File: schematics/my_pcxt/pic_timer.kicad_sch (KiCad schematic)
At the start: 4 parts, among them J3 Conn_02x40_Top_Bottom, P3 Conn_01x10, U15 8253, U7 8259A

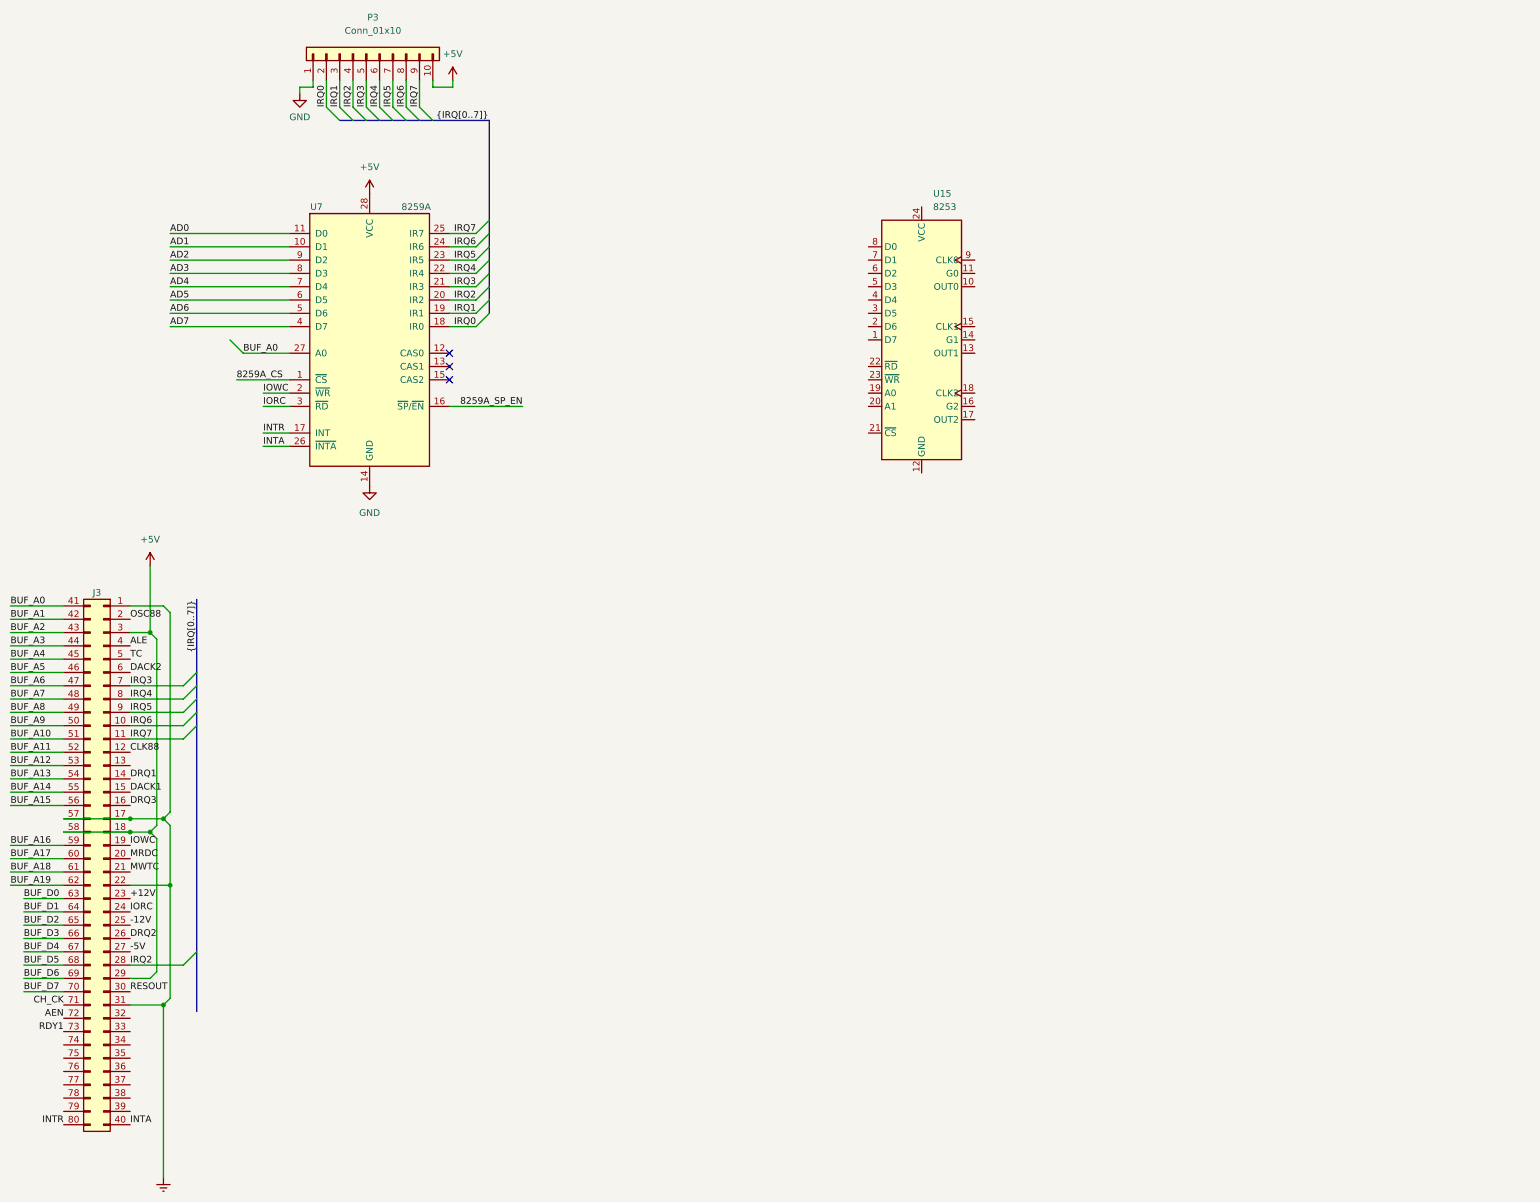
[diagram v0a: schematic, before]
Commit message: Implemented 8259 e 8253
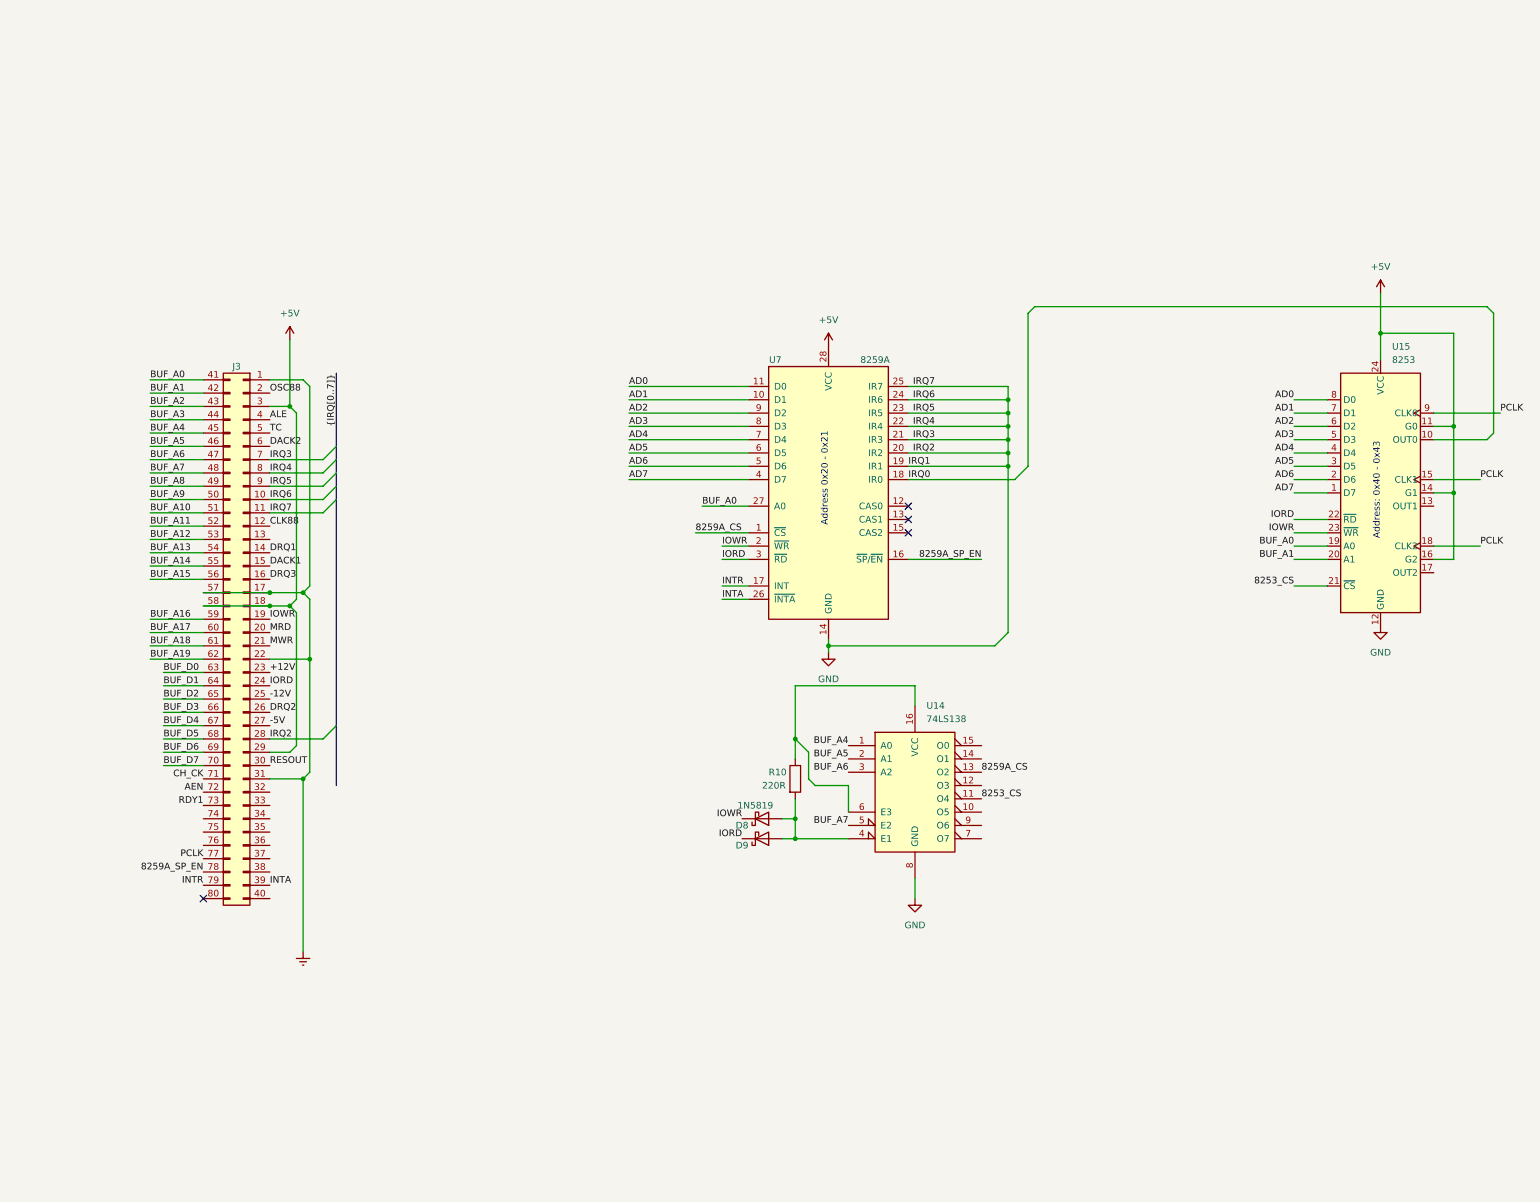
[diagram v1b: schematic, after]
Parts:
- removed P3: Conn_01x10, Connector_PinSocket_2.54mm:PinSocket_1x10_P2.54mm_Vertical, symbol Connector_Generic:Conn_01x10
- added D8, D9: 1N5819, Diode_THT:D_DO-41_SOD81_P10.16mm_Horizontal, symbol Diode:1N5819
- added R10: 220R, symbol Device:R
- added U14: 74LS138, symbol 74xx:74LS138
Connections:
- net IORC is gone; now on net IORD: J3.24 (Pin_24), U7.3 (~{RD})
- net IOWC is gone; now on net IOWR: J3.19 (Pin_19), U7.2 (~{WR})
- net IRQ1 is gone; now on net GND: U7.19 (IR1)
- net IRQ2 is gone; now on net GND: J3.28 (Pin_28), U7.20 (IR2)
- net IRQ3 is gone; now on net GND: J3.7 (Pin_7), U7.21 (IR3)
- net IRQ4 is gone; now on net GND: J3.8 (Pin_8), U7.22 (IR4)
- net IRQ5 is gone; now on net GND: J3.9 (Pin_9), U7.23 (IR5)
- net IRQ6 is gone; now on net GND: J3.10 (Pin_10), U7.24 (IR6)
- net IRQ7 is gone; now on net GND: J3.11 (Pin_11), U7.25 (IR7)
- net +5V: now also U15.11 (G0), U15.14 (G1), U15.16 (G2), U15.24 (VCC)
- net 8259A_CS: now also U14.13 (O2)
- net 8259A_SP_EN: now also J3.78 (Pin_78)
- net AD0: now also U15.8 (D0)
- net AD1: now also U15.7 (D1)
- net AD2: now also U15.6 (D2)
- net AD3: now also U15.5 (D3)
- net AD4: now also U15.4 (D4)
- net AD5: now also U15.3 (D5)
- net AD6: now also U15.2 (D6)
- net AD7: now also U15.1 (D7)
- net BUF_A0: now also U15.19 (A0)
- net BUF_A1: now also U15.20 (A1)
- net BUF_A4: now also U14.1 (A0)
- net BUF_A5: now also U14.2 (A1)
- net BUF_A6: now also U14.3 (A2)
- net BUF_A7: now also U14.5 (E2)
- net GND: now also U15.12 (GND), U14.8 (GND)
- net INTA: now also J3.39 (Pin_39); no longer J3.40 (Pin_40)
- net INTR: now also J3.79 (Pin_79); no longer J3.80 (Pin_80)
- net IRQ0: now also U15.10 (OUT0)
- net PCLK: now reaches U15.15 (CLK1)
- net PCLK: now also J3.77 (Pin_77), U15.18 (CLK2), U15.9 (CLK0)
- net 8253_CS: now reaches U15.21 (~{CS})
- net 8253_CS: now also U14.11 (O4)
- net IORD: now reaches U15.22 (~{RD})
- net IORD: now also D9.1 (K)
- net IOWR: now reaches U15.23 (~{WR})
- net IOWR: now also D8.1 (K)
- net MRDC renamed MRD
- net MWTC renamed MWR
- new net: R10.1, U14.16 (VCC), U14.6 (E3)
- new net: D8.2 (A), D9.2 (A), R10.2, U14.4 (E1)
- no-connect marks 3 -> 4
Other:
- note added: "Address 0x20 - 0x21"
- note added: "Address: 0x40 - 0x43"
- moved on the sheet: J3, U15, U7

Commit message: Updating schematics
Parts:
- removed D8, D9: 1N5819, Diode_THT:D_DO-41_SOD81_P10.16mm_Horizontal, symbol Diode:1N5819
- removed R10: 220R, symbol Device:R
- removed U14: 74LS138, symbol 74xx:74LS138
- added C12: 100nF, symbol Device:C
- added C19, C20, C21, C2VS+1, C2VS-1: 1uF, symbol Device:C_Polarized
- added D10, D5: 1N5819, Diode_THT:D_DO-41_SOD81_P10.16mm_Horizontal, symbol Diode:1N5819
- added J5: DE9_Plug, symbol Connector:DE9_Plug
- added R2: 270R, symbol Device:R
- added U14: 16550, Package_DIP:DIP-40_W15.24mm, symbol Interface_UART:16550
- added U23: DTE, symbol Interface_UART:MAX232
- added U3: PAL20L8, symbol Logic_Programmable:PAL20L8
- added X1: 4.915200MHz, Oscillator:Oscillator_DIP-14, symbol Oscillator:CXO_DIP14
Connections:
- net +5V: now also C12.1, C20.1, C2VS+1.2, R2.2, U14.25 (~{ADS}), U14.39 (~{RI}), U14.40 (VCC), U23.16 (VCC), U3.24 (VCC), X1.14 (Vcc)
- net 8253_CS: now also U3.21 (IO21)
- net 8259A_CS: now also U3.22 (IO22)
- net GNDREF: now also C12.2, C20.2, C2VS-1.1, U14.19 (WR), U14.22 (RD), U14.36 (~{CTS}), U14.37 (~{DSR}), U14.38 (~{DCD}), U23.15 (GND), U3.12 (GND), X1.7 (GND)
- net 8255_CS: now reaches J3.76 (Pin_76)
- net 8255_CS: now also U3.20 (I020)
- new net: D10.2 (A), D5.2 (A), R2.1, U3.8 (I8)
- new net: C2VS-1.2, U23.6 (VS-)
- new net: C19.1, U23.1 (C1+)
- new net: C19.2, U23.3 (C1-)
- new net: U14.10 (SIN), U23.9 (R2OUT)
- new net: U14.11 (SOUT), U23.10 (T2IN)
- new net: U14.15 (~{BAUDOUT}), U14.9 (RCLK)
- new net: C21.1, U23.4 (C2+)
- new net: C21.2, U23.5 (C2-)
- new net: C2VS+1.1, U23.2 (VS+)
- new net: J5.3, U23.7 (T2OUT)
- new net: J5.2, U23.8 (R2IN)
- new net A0: U14.28 (A0)
- new net A1: U14.27 (A1)
- new net A10: U3.4 (I4)
- new net A11: U3.10 (I10)
- new net A12: U3.11 (I11)
- new net A13: U3.13 (I13)
- new net A14: U3.14 (I14)
- new net A15: U3.23 (I23)
- new net A2: U14.26 (A2)
- new net A3: U14.12 (CS0), U3.1 (I1)
- new net A4: U14.13 (CS1), U3.5 (I5)
- new net A5: U3.6 (I6)
- new net A6: U3.7 (I7)
- new net A7: U3.9 (I9)
- new net A8: U3.2 (I2)
- new net A9: U3.3 (I3)
- new net CLOCK: U14.16 (XIN), X1.8 (OUT)
- new net COM1_CS: U14.14 (~{CS2}), U3.18 (IO18)
- new net D0: U14.1 (D0)
- new net D1: U14.2 (D1)
- new net D2: U14.3 (D2)
- new net D3: U14.4 (D3)
- new net D4: U14.5 (D4)
- new net D5: U14.6 (D5)
- new net D6: U14.7 (D6)
- new net D7: U14.8 (D7)
- new net LPT1_CS: U3.19 (IO19)
- new net RESET: U14.35 (MR)
- new net /IOR: D5.1 (K)
- new net /IORD: U14.21 (~{RD})
- new net /IOW: D10.1 (K)
- new net /IOWR: U14.18 (~{WR})
- no-connect marks 4 -> 18
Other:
- note added: "Serial msdos address.. COM1: 3F8h COM2: 2F8h"
- moved on the sheet: J3, U15, U7
